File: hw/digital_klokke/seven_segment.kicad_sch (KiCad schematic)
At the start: 8 parts, among them U201 74LS47

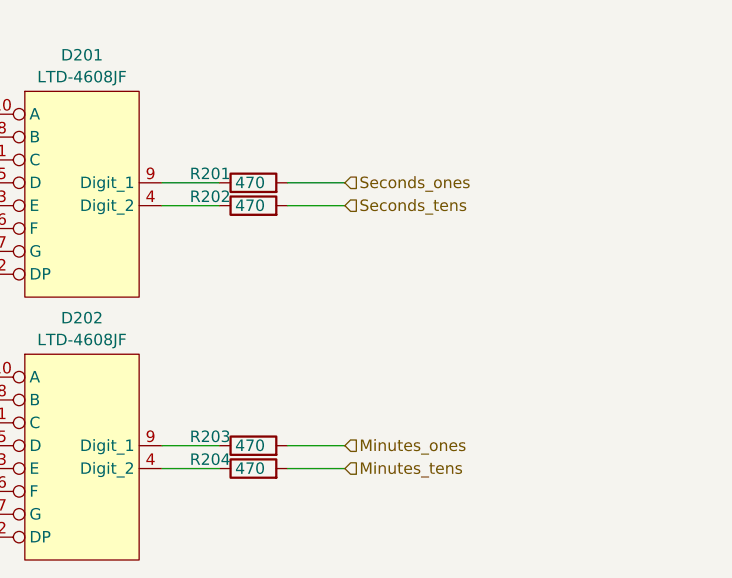
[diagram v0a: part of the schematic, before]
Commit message: added segment display footprint
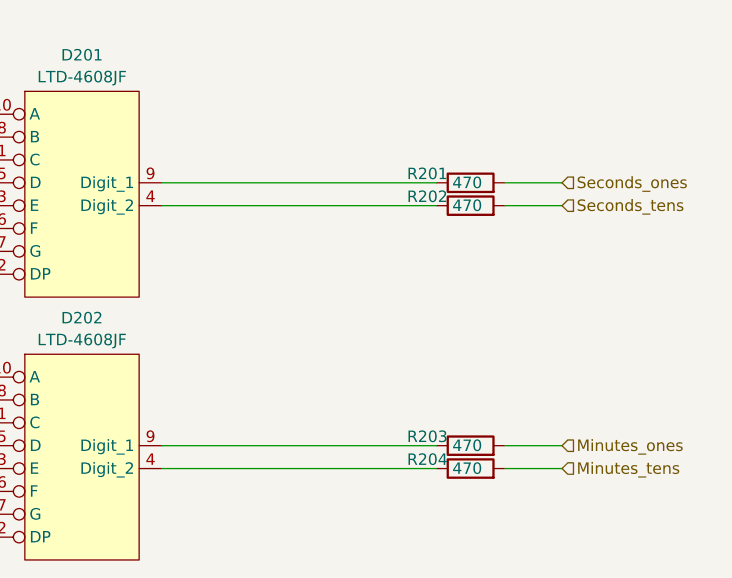
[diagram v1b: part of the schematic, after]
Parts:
- D201, D202: footprint (none) -> OMG_Optoelectronics:Lite-On LTD-4608JF
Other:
- moved on the sheet: R201, R202, R203, R204

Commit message: final design changes. Design freeze
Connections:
- net +5V: no longer D201.2 (DP), D202.2 (DP)
- new net nDP: D201.2 (DP), D202.2 (DP)
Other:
- title: (none) -> Digital Klokke
- moved on the sheet: C201, D201, D202, R201, R202, R203, R204, U201

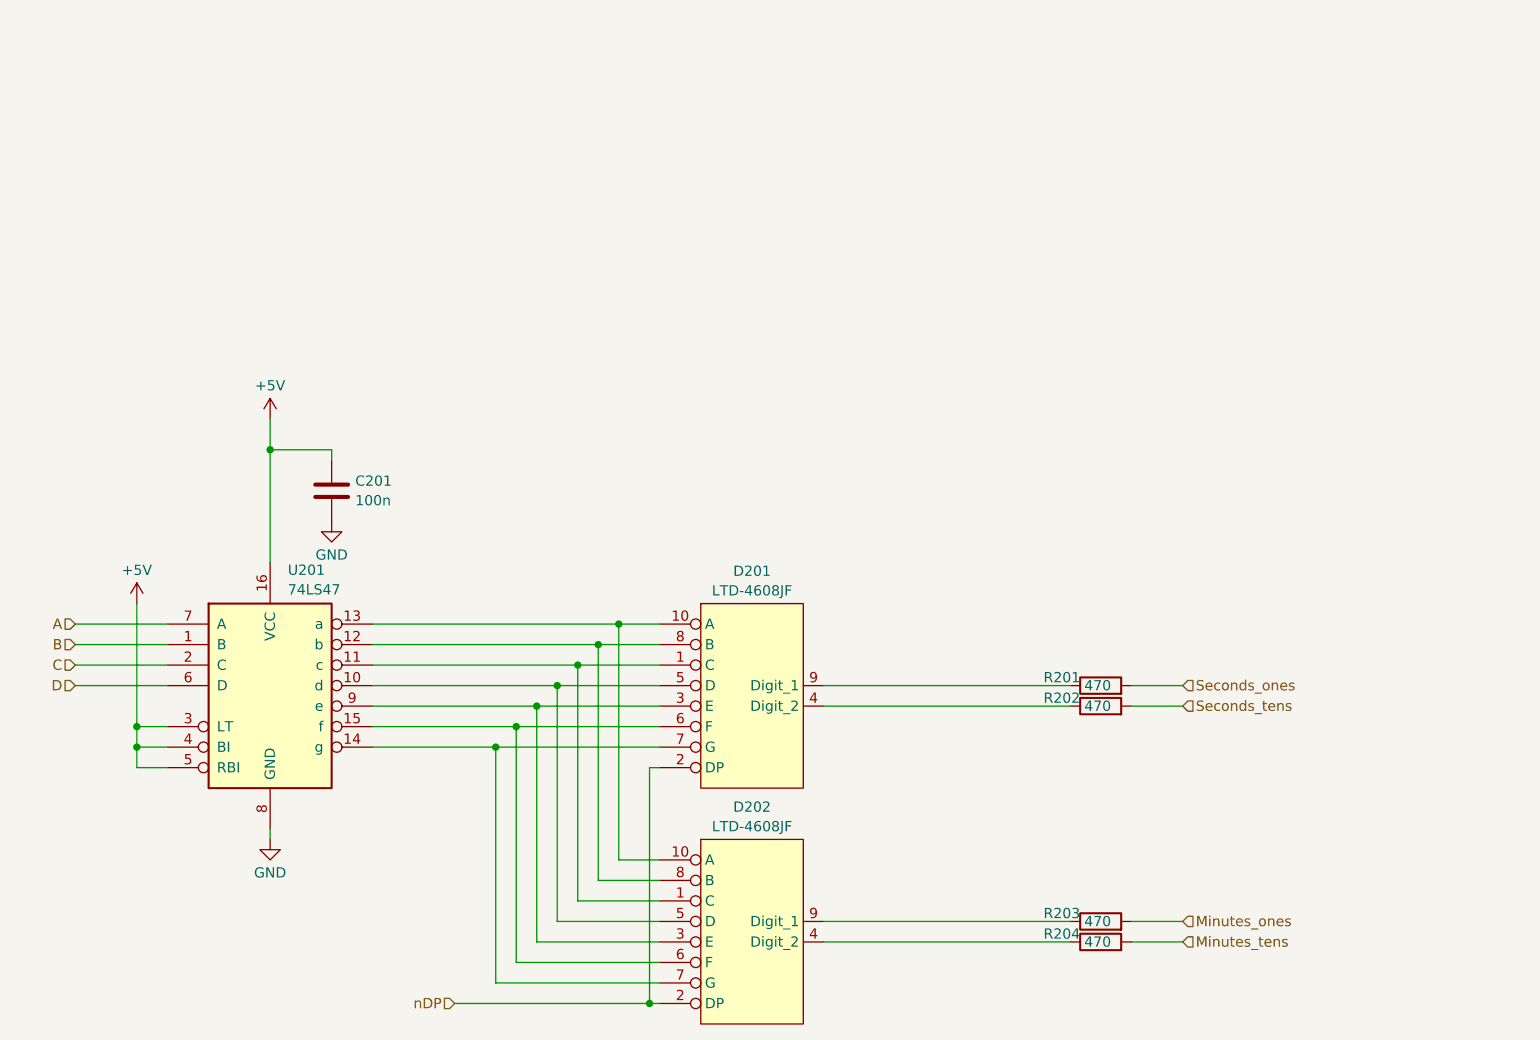
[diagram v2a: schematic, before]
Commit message: added resistor to each cathode
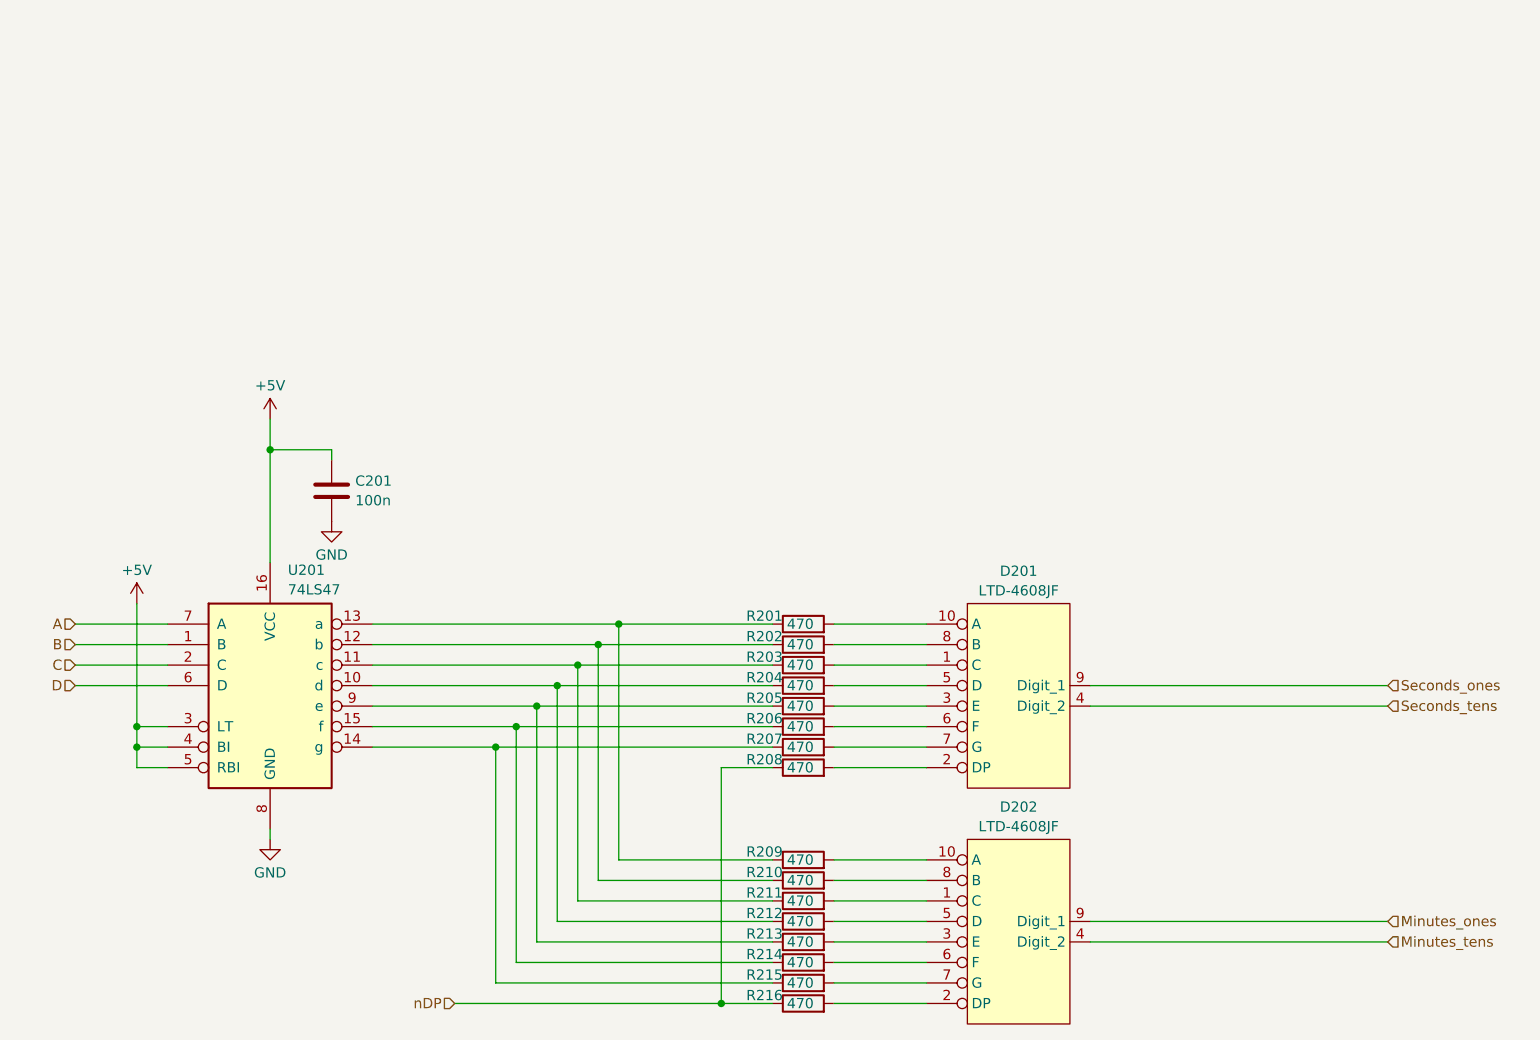
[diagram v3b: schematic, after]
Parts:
- added R205, R206, R207, R208, R209, R210, R211, R212, R213, R214, R215, R216: 470, Resistor_SMD:R_0805_2012Metric_Pad1.20x1.40mm_HandSolder, symbol Device:R
- R201, R202, R203, R204: footprint Resistor_THT:R_Axial_DIN0207_L6.3mm_D2.5mm_P10.16mm_Horizontal -> Resistor_SMD:R_0805_2012Metric_Pad1.20x1.40mm_HandSolder
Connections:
- net Minutes_ones: now also D202.9 (Digit_1); no longer R203.2
- net Minutes_tens: now also D202.4 (Digit_2); no longer R204.2
- net Seconds_ones: now also D201.9 (Digit_1); no longer R201.2
- net Seconds_tens: now also D201.4 (Digit_2); no longer R202.2
- net nDP: now also R208.1, R216.1; no longer D201.2 (DP), D202.2 (DP)
- net at R203.1: now also U201.11 (c), R211.1; no longer D202.9 (Digit_1)
- net at R202.1: now also U201.12 (b), R210.1; no longer D201.4 (Digit_2)
- net at R201.1: now also U201.13 (a), R209.1; no longer D201.9 (Digit_1)
- net at R204.1: now also U201.10 (d), R212.1; no longer D202.4 (Digit_2)
- new net: R207.1, R215.1, U201.14 (g)
- new net: D202.7 (G), R215.2
- new net: D201.1 (C), R203.2
- new net: D201.10 (A), R201.2
- new net: D201.2 (DP), R208.2
- new net: D201.3 (E), R205.2
- new net: D201.5 (D), R204.2
- new net: D201.6 (F), R206.2
- new net: D201.7 (G), R207.2
- new net: D201.8 (B), R202.2
- new net: R205.1, R213.1, U201.9 (e)
- new net: D202.10 (A), R209.2
- new net: D202.5 (D), R212.2
- new net: R206.1, R214.1, U201.15 (f)
- new net: D202.2 (DP), R216.2
- new net: D202.8 (B), R210.2
- new net: D202.3 (E), R213.2
- new net: D202.1 (C), R211.2
- new net: D202.6 (F), R214.2
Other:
- moved on the sheet: D201, D202
